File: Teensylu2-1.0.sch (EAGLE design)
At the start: 114 parts, among them J1 M02POLAR, J10 HOTEND-2, J11 M02POLAR, J12 M02POLAR, J13 M02POLAR, J2 MICROSD, J3 USB-MICRO-PTH, J4 M02POLAR, J5 4P-TERM-BLOCK284391-4, J6 39-29-3066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

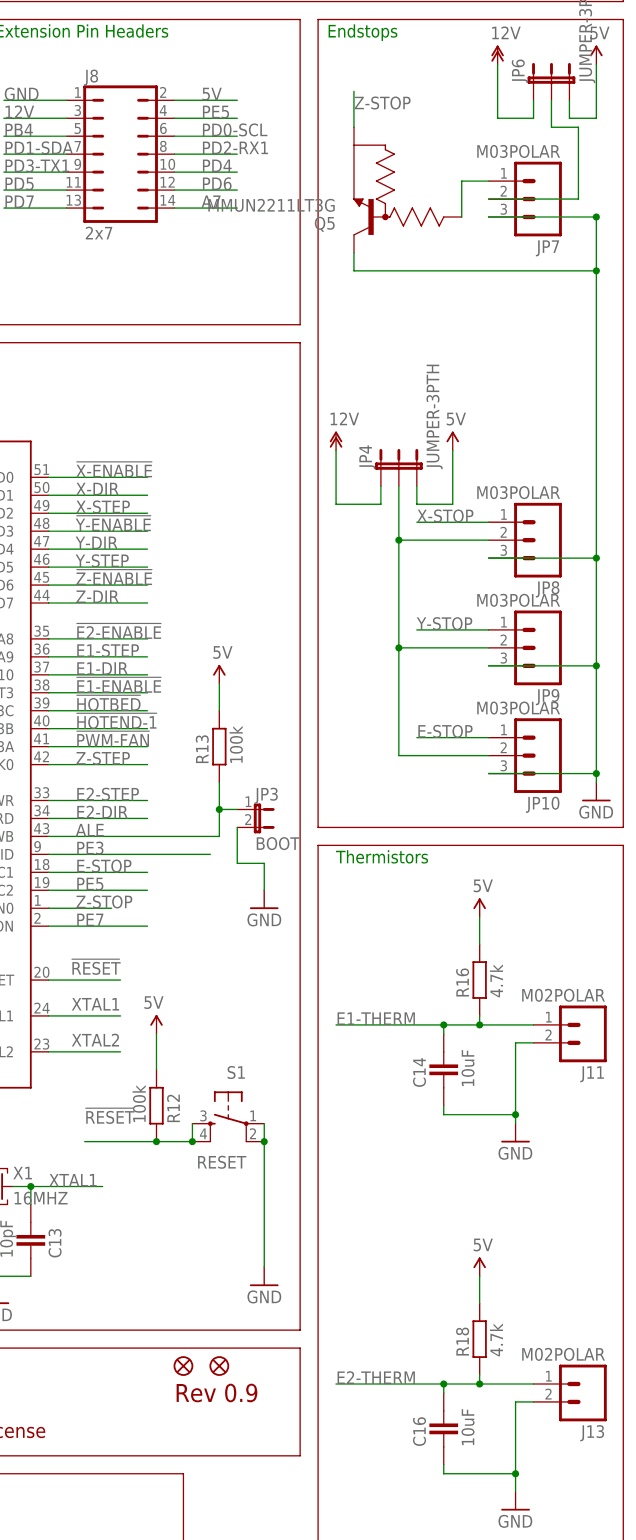
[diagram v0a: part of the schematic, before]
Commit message: Fixed Z Endstop
Collector and Emitter were swapped.
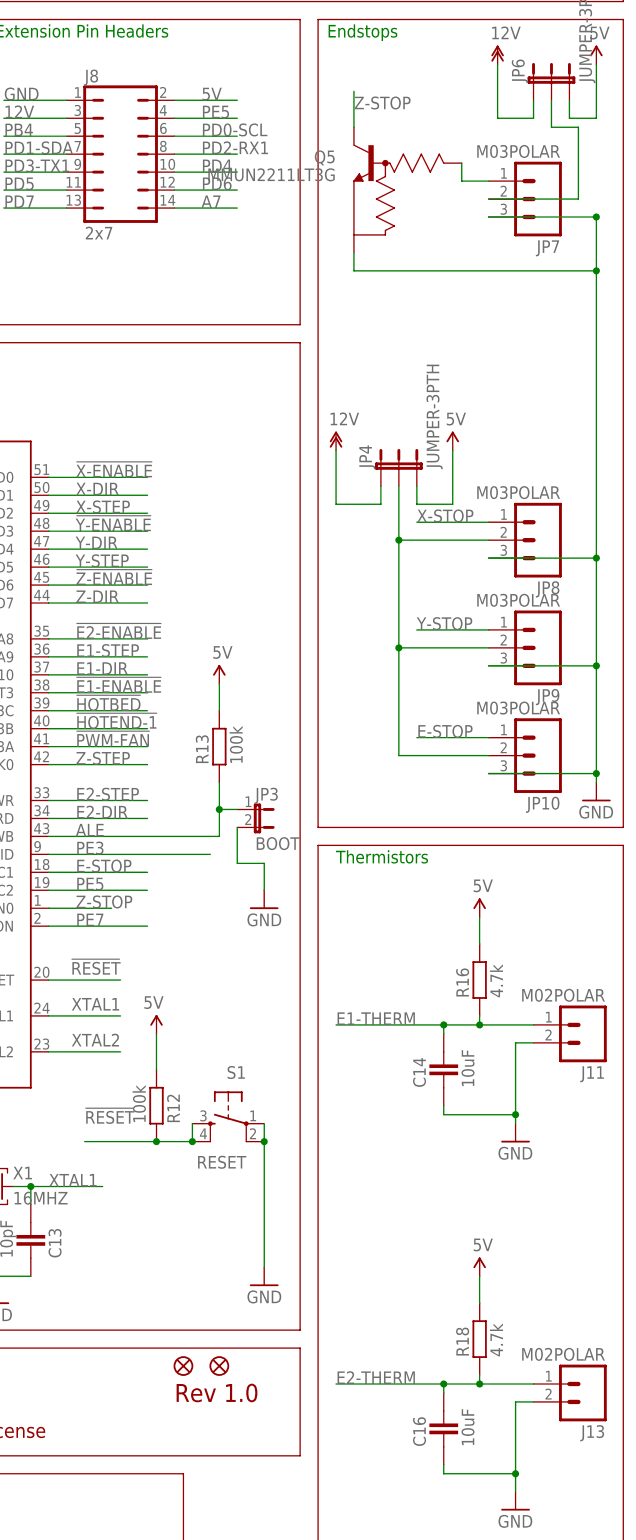
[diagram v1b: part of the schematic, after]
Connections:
- net GND: now also Q5.E; no longer Q5.C
- net Z-STOP: now also Q5.C; no longer Q5.E
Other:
- note added: "Rev 1.0"
- note removed: "Rev 0.9"
- moved on the sheet: Q5
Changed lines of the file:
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@@
 <setting verticaltext="up"/>
 </settings>
-<grid distance="50" unitdist="mil" unit="mil" style="lines" multiple="1" display="no" altdistance="0.01" altunitdist="inch" altunit="inch"/>
+<grid distance="0.1" unitdist="inch" unit="inch" style="lines" multiple="1" display="no" altdistance="0.01" altunitdist="inch" altunit="inch"/>
 <layers>
 <layer number="1" name="Top" color="4" fill="1" visible="no" active="no"/>
@@
 <text x="10.16" y="149.86" size="1.778" layer="91" font="vector">Power Acc</text>
 <text x="60.96" y="7.62" size="3.81" layer="94">Teensylu2</text>
-<text x="175.26" y="7.62" size="2.54" layer="94">Rev 0.9</text>
+<text x="175.26" y="7.62" size="2.54" layer="94">Rev 1.0</text>
 <text x="111.76" y="7.62" size="3.048" layer="94">Control for Reprap</text>
 <text x="63.5" y="2.54" size="2.032" layer="94">Licensed under the Creative Commons Attributions ShareAlike 3.0 License</text>
@@
 <attribute name="NOTES" x="233.68" y="10.16" size="1.778" layer="96" rot="R180" display="off"/>
 </instance>
-<instance part="Q5" gate="G$1" x="203.2" y="175.26" rot="R180">
-<attribute name="DESCRIPTION" x="203.2" y="175.26" size="1.778" layer="96" rot="R180" display="off"/>
-<attribute name="MANUFACTURER" x="203.2" y="175.26" size="1.778" layer="96" rot="R180" display="off"/>
-<attribute name="MANUFACTURER_PART_NUMBER" x="203.2" y="175.26" size="1.778" layer="96" rot="R180" display="off"/>
+<instance part="Q5" gate="G$1" x="203.2" y="182.88" rot="MR0">
+<attribute name="DESCRIPTION" x="203.2" y="182.88" size="1.778" layer="96" rot="MR0" display="off"/>
+<attribute name="MANUFACTURER" x="203.2" y="182.88" size="1.778" layer="96" rot="MR0" display="off"/>
+<attribute name="MANUFACTURER_PART_NUMBER" x="203.2" y="182.88" size="1.778" layer="96" rot="MR0" display="off"/>
 </instance>
 </instances>
@@
 <pinref part="JP10" gate="G$1" pin="3"/>
 <junction x="234.95" y="127"/>
-<pinref part="Q5" gate="G$1" pin="C"/>
-<wire x1="200.66" y1="170.18" x2="200.66" y2="167.64" width="0.1524" layer="91"/>
 <wire x1="200.66" y1="167.64" x2="234.95" y2="167.64" width="0.1524" layer="91"/>
 <junction x="234.95" y="167.64"/>
+<pinref part="Q5" gate="G$1" pin="E"/>
+<wire x1="200.66" y1="167.64" x2="200.66" y2="170.18" width="0.1524" layer="91"/>
 </segment>
 <segment>
@@
 <net name="Z-STOP" class="0">
 <segment>
-<pinref part="Q5" gate="G$1" pin="E"/>
-<wire x1="200.66" y1="187.96" x2="200.66" y2="193.04" width="0.1524" layer="91"/>
 <label x="200.66" y="190.5" size="1.778" layer="95"/>
+<pinref part="Q5" gate="G$1" pin="C"/>
+<wire x1="200.66" y1="187.96" x2="200.66" y2="193.04" width="0.1524" layer="91"/>
 </segment>
 <segment>
@@
 <pinref part="JP7" gate="G$1" pin="1"/>
 <pinref part="Q5" gate="G$1" pin="B"/>
-<wire x1="215.9" y1="180.34" x2="215.9" y2="175.26" width="0.1524" layer="91"/>
+<wire x1="215.9" y1="180.34" x2="215.9" y2="182.88" width="0.1524" layer="91"/>
 </segment>
 </net>
